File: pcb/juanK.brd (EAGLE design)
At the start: 100 x 80 mm, 56 parts, among them IC1 MEGA8-P, IC2 7805TV, T1 2N3904, T2 MCR106, T3 MCR106, T4 MCR106, T5 MCR106, T6 MCR106, T7 MCR106

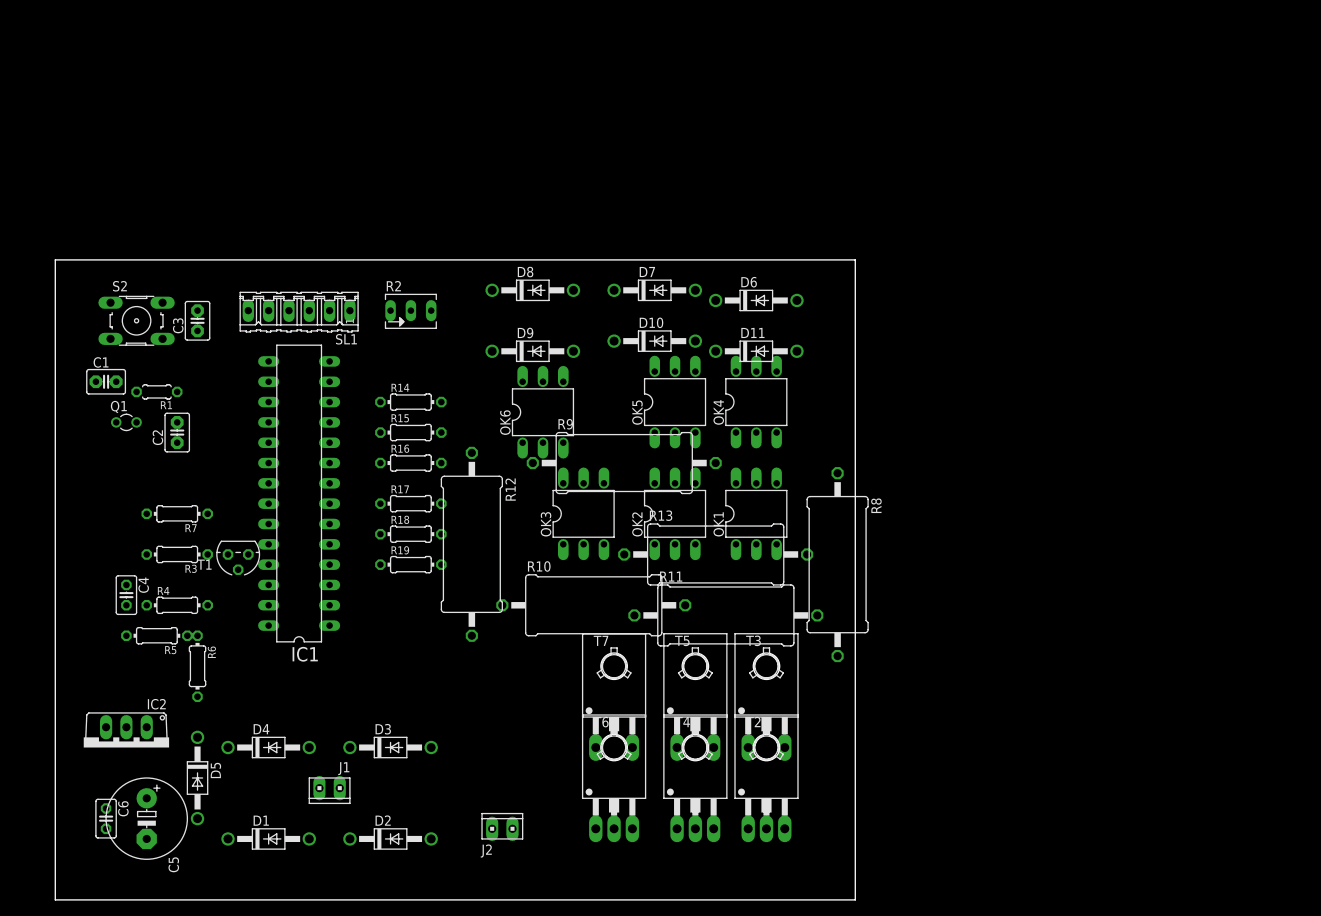
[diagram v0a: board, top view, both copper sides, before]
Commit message: Ordenar elementos y Optimizar caminos
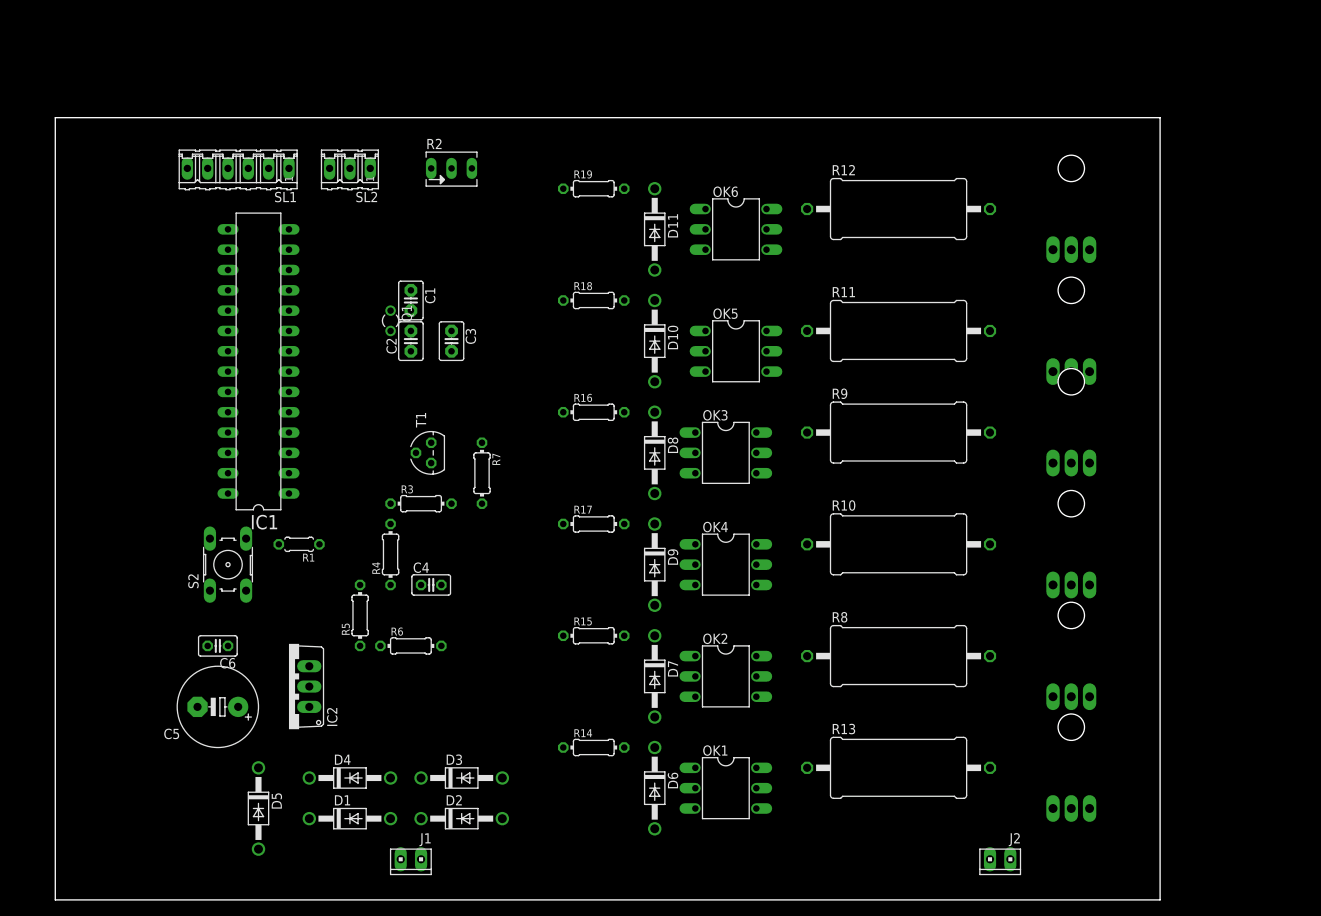
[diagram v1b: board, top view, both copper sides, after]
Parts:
- added SL2: (no value), con-amp-quick:03P
- moved T7 84.5 mm to (127.0, 86.4), flipped to the bottom
- moved T6 80.8 mm to (127.0, 71.1), flipped to the bottom
- moved R12 67.8 mm to (105.4, 86.4), turned to 0 degrees
- moved T4 65.6 mm to (127.0, 59.7), flipped to the bottom
- moved J2 62.3 mm to (118.1, 5.08), turned to 180 degrees
- moved D6 62.3 mm to (74.9, 14.0), turned to 270 degrees
- moved R19 52.3 mm to (67.3, 88.9)
- moved T5 51.2 mm to (127.0, 44.5), flipped to the bottom
- moved R14 48.9 mm to (67.3, 19.1)
- moved D7 48.3 mm to (74.9, 27.9), turned to 270 degrees
- moved R11 41.6 mm to (105.4, 71.1)
- moved C1 39.4 mm to (44.5, 74.9), turned to 270 degrees
- moved R10 38.9 mm to (105.4, 44.5)
- moved T3 38.6 mm to (127.0, 30.5), flipped to the bottom
- moved R7 38.4 mm to (53.3, 53.3), turned to 270 degrees
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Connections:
- net S1_S2: now also SL2.1
- net S3_S4: now also SL2.2
- net S5_S6: now also SL2.3
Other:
- board size 100 x 80 mm -> 138.1 x 97.8 mm

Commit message: Diseño de PCB terminado
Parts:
- added JP1, JP10, JP11, JP12, JP13, JP14, JP15, JP16, JP17, JP18, JP19, JP2, JP20, JP21, JP22, JP23, JP24, JP3, JP4, JP5, JP6, JP7, JP8, JP9: (no value), pinhead:1X01
- J1, J2: device con-amp:10X02MTA -> con-lstb:MA03-1
- SL1: device con-amp-quick:06P -> con-amp:10X06MTA
- SL2: device con-amp-quick:03P -> con-amp:10X04MTA
- T2, T3, T4, T5, T6, T7: value MCR106 -> TIC106S; device triac:TO126L -> triac:TIC106S
- moved R2 46.6 mm to (8.89, 68.6), turned to 270 degrees
- moved T2 30.9 mm to (121.9, 47.0), turned to 270 degrees
- moved T6 25.3 mm to (119.4, 95.2), turned to 270 degrees
- moved D6 25.0 mm to (64.8, 36.8)
- moved R13 25.0 mm to (95.2, 39.4)
- moved R14 25.0 mm to (57.1, 41.9)
- moved OK1 24.5 mm to (74.9, 36.8)
- moved D10 23.9 mm to (64.8, 91.4)
- moved OK5 23.9 mm to (74.9, 90.2)
- moved T5 23.9 mm to (137.2, 66.0), turned to 270 degrees
- moved R18 23.9 mm to (57.1, 96.5)
- moved R11 23.9 mm to (95.2, 92.7)
- moved C6 19.8 mm to (7.62, 16.5), turned to 270 degrees
- moved T3 19.4 mm to (137.2, 47.0), turned to 270 degrees
- moved IC2 16.6 mm to (12.7, 25.4), turned to 180 degrees
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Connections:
- removed net N$13: T2.C, T4.C, T6.C
- new net VO: JP23.1, JP24.1, T2.C, T4.C, T6.C
- net A: now also JP15.1, JP16.1
- net B: now also J2.3, JP11.1, JP12.1, JP17.1, JP18.1; no longer J2.2
- net C: now also JP19.1, JP20.1
- net GND: now also JP13.1, JP14.1, SL2.4
- net GND1: now also JP21.1, JP22.1
- net N$11: now also J1.3; no longer J1.2
- net N$22: now also JP5.1, JP6.1
- net N$24: now also JP7.1, JP8.1
- net N$25: now also JP3.1, JP4.1
- net N$6: now also JP10.1, JP9.1
- net N$8: now also JP1.1, JP2.1
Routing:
- net 5V: track 0.00 -> 272.0 mm
- net B: track 0.00 -> 128.3 mm
- net VO: track 0.00 -> 114.3 mm
- net A: track 0.00 -> 108.0 mm
- net N$20: track 0.00 -> 104.1 mm
- net S1_S2: track 0.00 -> 90.2 mm
- net S3_S4: track 0.00 -> 87.6 mm
- net N$25: track 0.00 -> 85.1 mm
- net C: track 0.00 -> 77.5 mm
- net N$24: track 0.00 -> 76.2 mm
- net S5_S6: track 0.00 -> 62.2 mm
- net N$6: track 0.00 -> 55.9 mm
- net N$22: track 0.00 -> 52.1 mm
- net N$8: track 0.00 -> 48.3 mm
- net GND: track 0.00 -> 44.4 mm
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- added copper zone on layer 16, net GND
- added copper zone on layer 16, net GND1
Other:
- board size 138.1 x 97.8 mm -> 155.9 x 110.5 mm

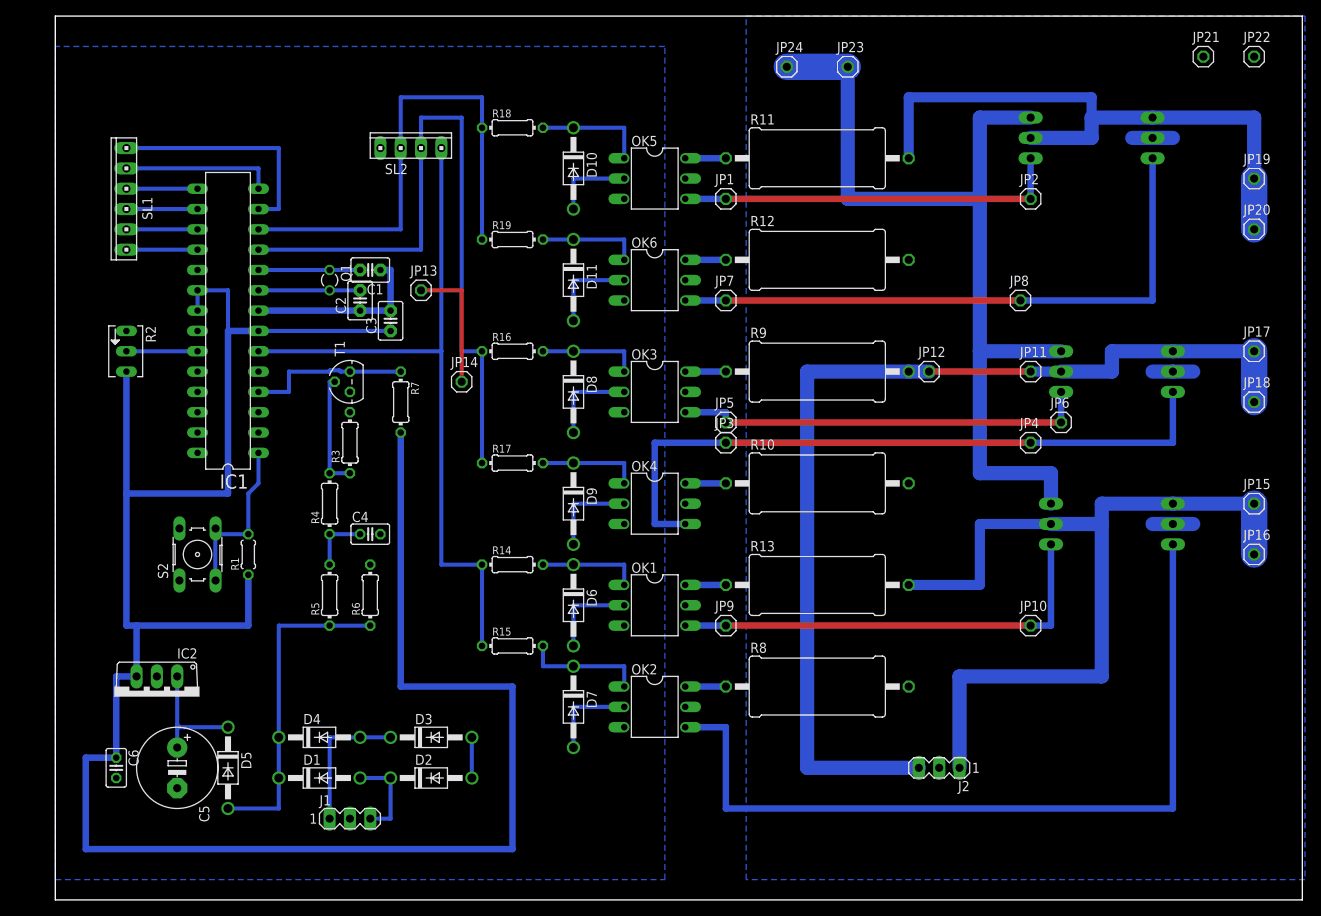
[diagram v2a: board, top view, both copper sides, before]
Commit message: Corregir dimensiones de algunos componentes
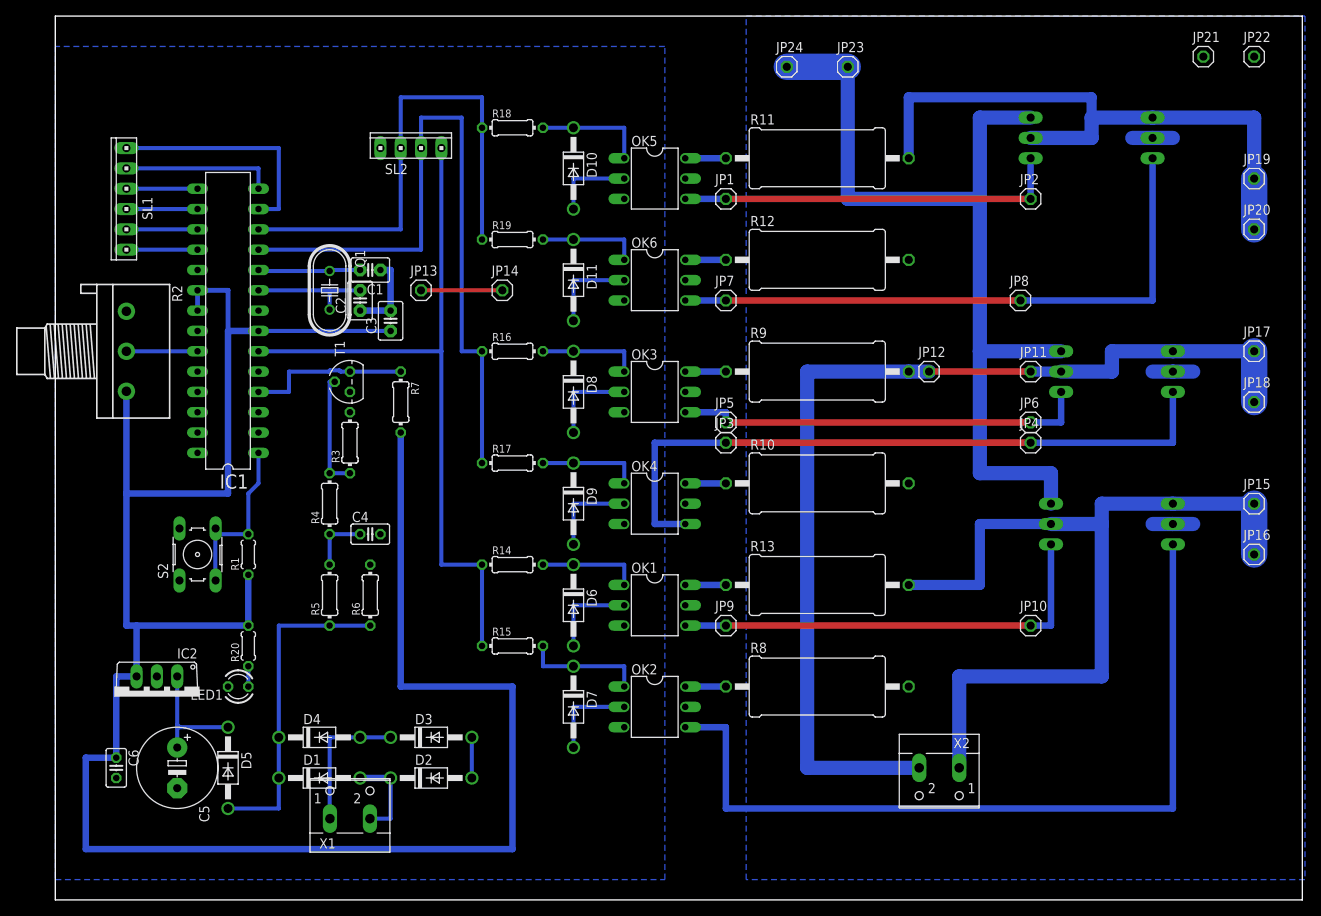
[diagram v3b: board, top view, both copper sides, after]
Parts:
- removed J1, J2: (no value), con-lstb:MA03-1
- added LED1: (no value), led:LED3MM
- added R20: (no value), rcl:0204/5
- added X1, X2: (no value), con-wago-500:W237-102
- Q1: device crystal:TC26V -> crystal:HC49U70
- R2: device pot:B64Y -> pot:3RP/1610N
- moved JP14 12.5 mm to (55.9, 76.2)
- moved JP6 3.81 mm to (121.9, 59.7)
- moved Q1 1.27 mm to (34.3, 76.2)
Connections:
- new net N$13: LED1.A, R20.1
- net 5V: now also R2.3, R20.2; no longer R2.A
- net A: now also X2.1; no longer J2.1
- net B: now also X2.2; no longer J2.3
- net GND: now also LED1.K, R2.1; no longer R2.E
- net N$10: now also X1.1; no longer J1.1
- net N$11: now also X1.2; no longer J1.3
- net N$7: now also R2.2; no longer R2.S
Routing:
- net GND: track 44.4 -> 25.4 mm
- net N$11: track 11.8 -> 15.8 mm
- net N$13: track 0.00 -> 2.54 mm
- net N$14: track 12.7 -> 15.1 mm
- net 5V: track 272.0 -> 269.7 mm

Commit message: Incrementar espacio entre pista y tierra e incrementar ancho de las pistas
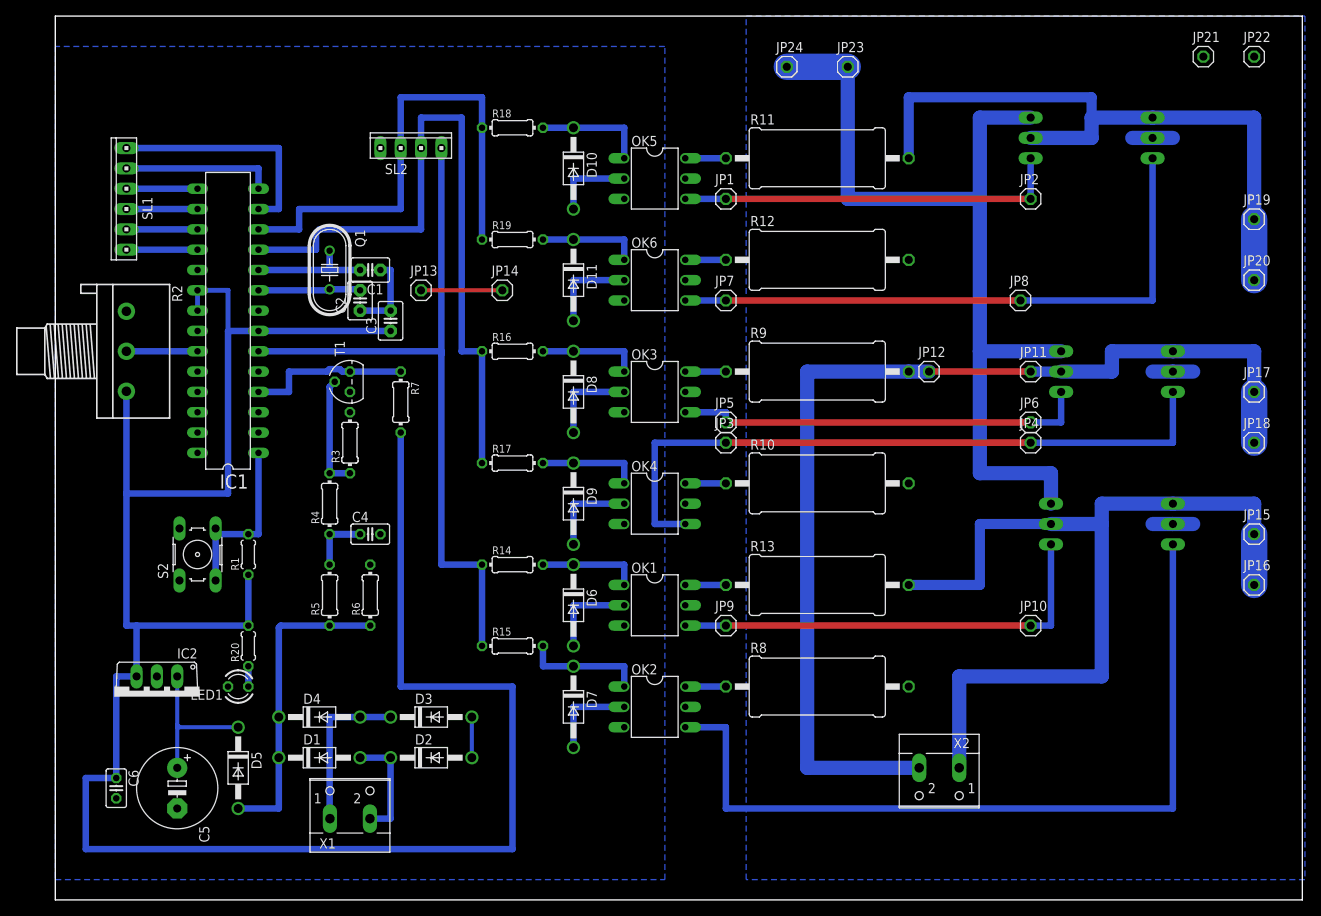
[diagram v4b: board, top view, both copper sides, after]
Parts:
- moved JP20 6.35 mm to (149.9, 77.5)
- moved JP17 5.08 mm to (149.9, 63.5)
- moved JP18 5.08 mm to (149.9, 57.1)
- moved JP19 5.08 mm to (149.9, 85.1)
- moved JP15 3.81 mm to (149.9, 45.7)
- moved JP16 3.81 mm to (149.9, 39.4)
- moved C5 2.54 mm to (15.2, 14.0)
- moved C6 2.54 mm to (7.62, 14.0)
- moved D1 2.54 mm to (33.0, 17.8)
- moved D2 2.54 mm to (47.0, 17.8)
- moved D3 2.54 mm to (47.0, 22.9)
- moved D4 2.54 mm to (33.0, 22.9)
- moved Q1 2.54 mm to (34.3, 78.7)
- moved D5 1.27 mm to (22.9, 16.5)
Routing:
- net S1_S2: track 90.2 -> 145.2 mm
- net N$5: track 40.6 -> 73.5 mm
- net N$32: track 12.7 -> 25.9 mm
- net N$28: track 12.7 -> 25.4 mm
- net C: track 77.5 -> 83.8 mm
- net B: track 128.3 -> 133.4 mm
- net N$1: track 7.62 -> 11.5 mm
- net A: track 108.0 -> 111.8 mm
- net N$3: track 15.4 -> 19.2 mm
- net N$10: track 17.8 -> 20.4 mm
- net N$14: track 15.1 -> 12.8 mm
- net N$15: track 13.0 -> 15.2 mm
- net N$11: track 15.8 -> 14.0 mm
